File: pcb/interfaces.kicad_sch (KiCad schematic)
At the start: 26 parts

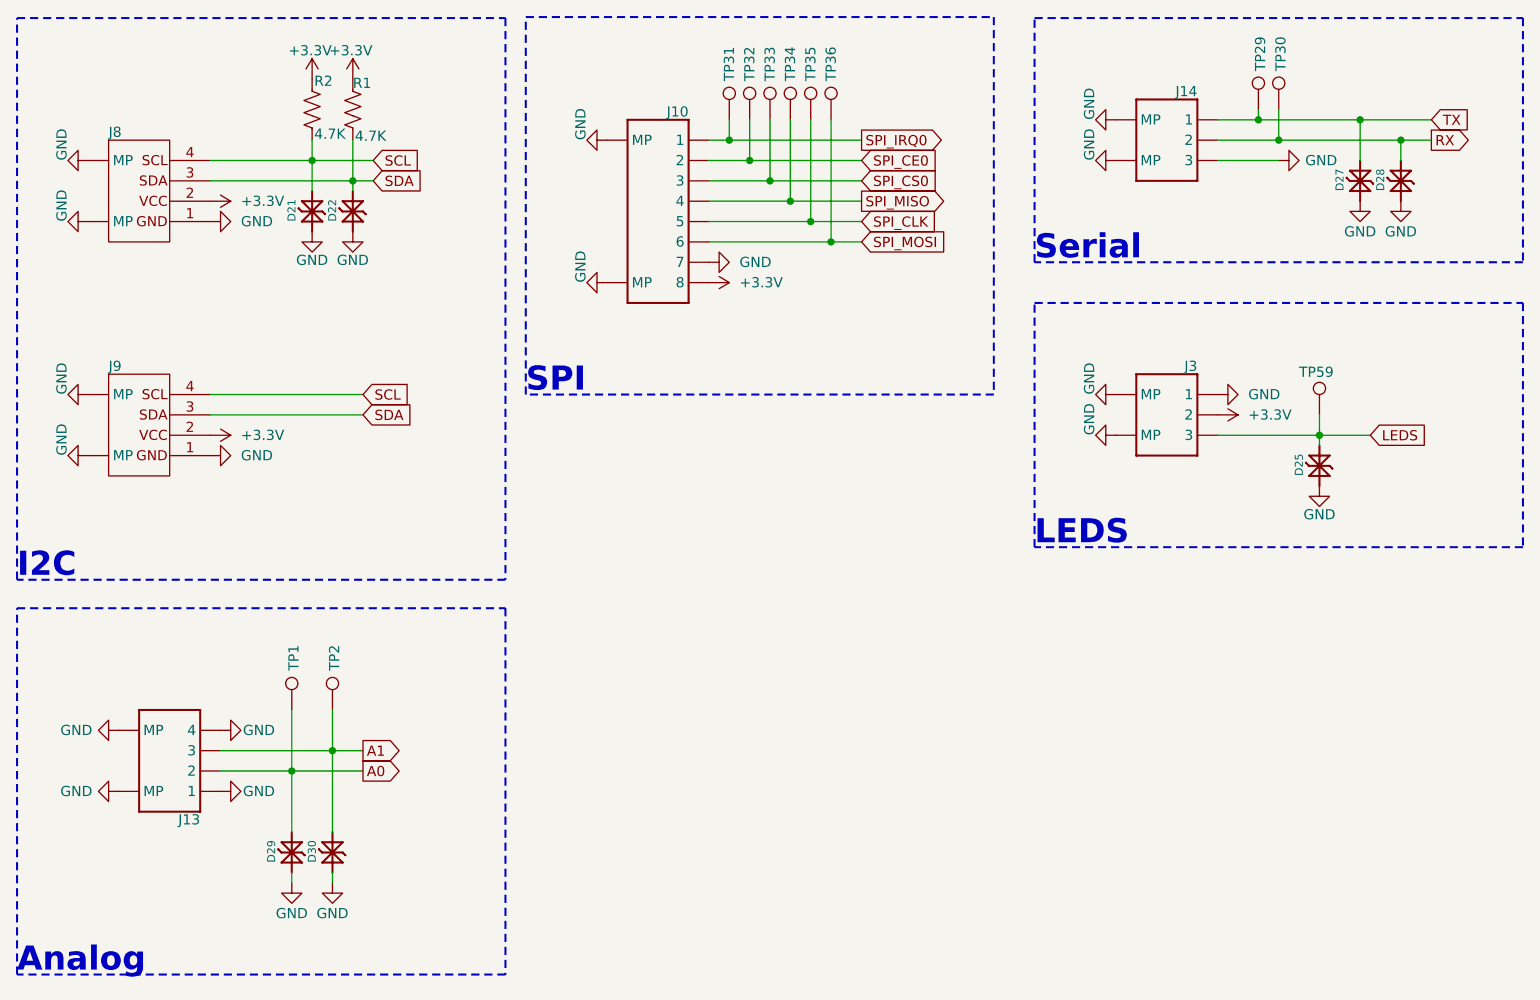
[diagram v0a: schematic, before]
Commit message: Renamed and added guard ring
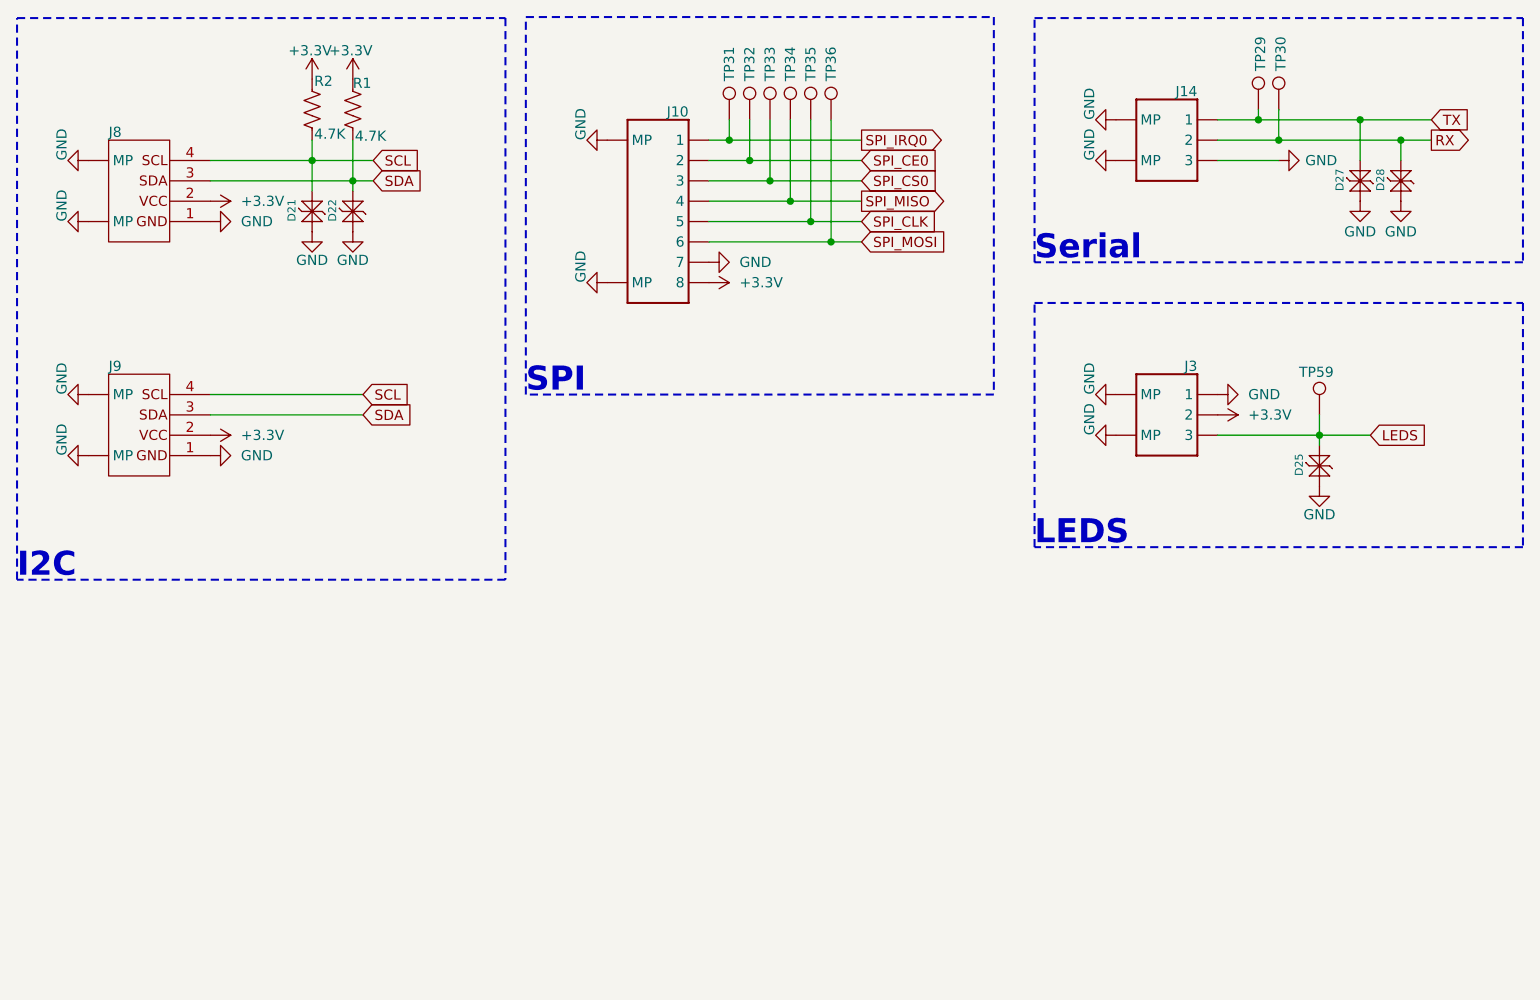
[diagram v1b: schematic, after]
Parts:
- removed D29, D30: PESD3V3S1BL, CRGM Passive:DFN1006-2, symbol CRGM Passive:PESD3V3S1BL
- removed J13: ~, CRGM Connector:JST_SH_BM04B-SRSS-TB_1x04-1MP_P1.00mm_Vertical, symbol CRGM Connector:JST-SH-4
- removed TP1, TP2: ~, CRGM Mechanical:TestPoint_Pad_D1.0mm, symbol Connector:TestPoint
- J10, J14, J3, J8, J9, TP29, TP30, TP31, TP32, TP33, TP34, TP35, TP36, TP59: value ~ -> (none)
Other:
- note removed: "Analog"
